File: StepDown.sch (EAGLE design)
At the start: 18 parts, among them IC1 TL494CN, T1 TIP32A

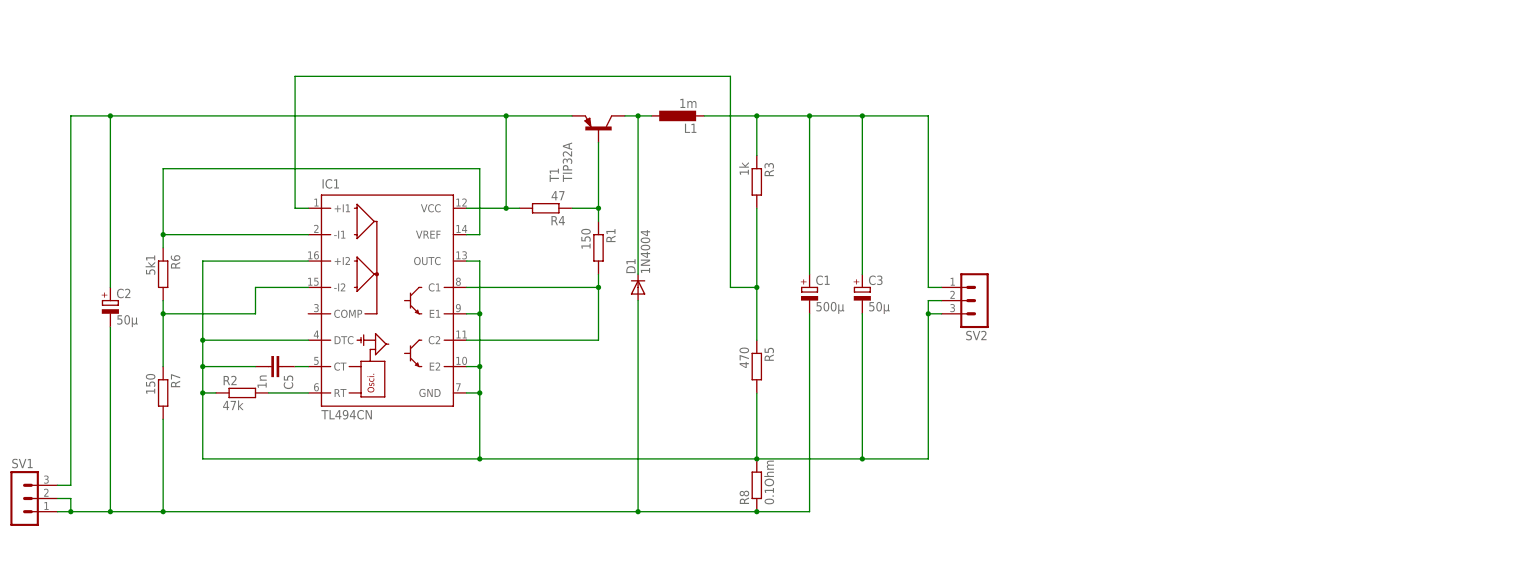
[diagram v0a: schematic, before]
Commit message: Add current sense (not tested)
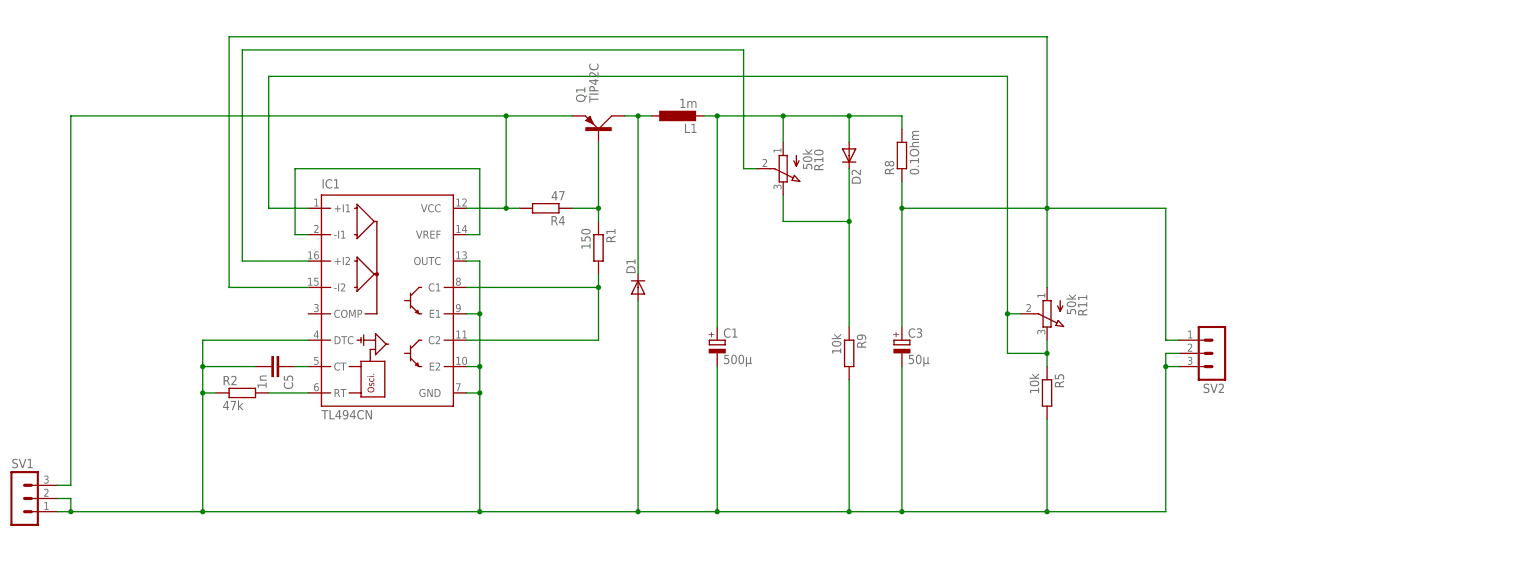
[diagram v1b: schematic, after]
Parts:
- removed C2: 50µ, rcl:CPOL-EUE5-8.5
- removed R3: 1k, rcl:R-EU_0204/2V
- removed R6: 5k1, rcl:R-EU_0204/2V
- removed R7: 150, rcl:R-EU_0204/2V
- removed T1: TIP32A, transistor:TIP32A
- added D2: (no value), diode:DIODE-D-2.5
- added Q1: TIP42C, transistor-power:TIP42C
- added R10, R11: 50k, pot:EVUE2A
- added R9: 10k, rcl:R-EU_0204/2V
- C3: device rcl:CPOL-EUE5-8.5 -> rcl:CPOL-EUE2.5-7
- D1: value 1N4004 -> (none); device diode:1N4004 -> diode:DIODE-D-2.5
- R5: value 470 -> 10k
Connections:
- removed net N$14: C3.-, C5.2, IC1.+I2, IC1.DTC, IC1.E1, IC1.E2, IC1.GND, IC1.OUTC, R2.1, R5.2, R8.2, SV2.2, SV2.3
- new net N$12: C1.-, C3.-, C5.2, D1.A, IC1.DTC, IC1.E1, IC1.E2, IC1.GND, IC1.OUTC, R2.1, R5.2, R9.2, SV1.1, SV1.2, SV2.2, SV2.3
- new net N$4: C1.+, D2.A, L1.2, R10.A, R8.2
- net N$1: now also Q1.E; no longer C2.+, T1.E
- net N$10: now also IC1.-I2, R11.A, R8.1; no longer C1.+, L1.2, R3.1
- net N$11: now also R11.E, R11.S; no longer R3.2
- net N$13: now also D2.C, R10.E, R9.1; no longer IC1.-I2, R6.2, R7.1
- net N$3: no longer R6.1
- net N$5: now also IC1.+I2, R10.S; no longer C1.-, C2.-, D1.A, R7.2, R8.1, SV1.1, SV1.2
- net N$7: now also Q1.B; no longer T1.B
- net N$9: now also Q1.C; no longer T1.C
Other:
- moved on the sheet: C1, C3, R5, R8, SV2

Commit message: Use MOSFET for more than 25A (tested and working)
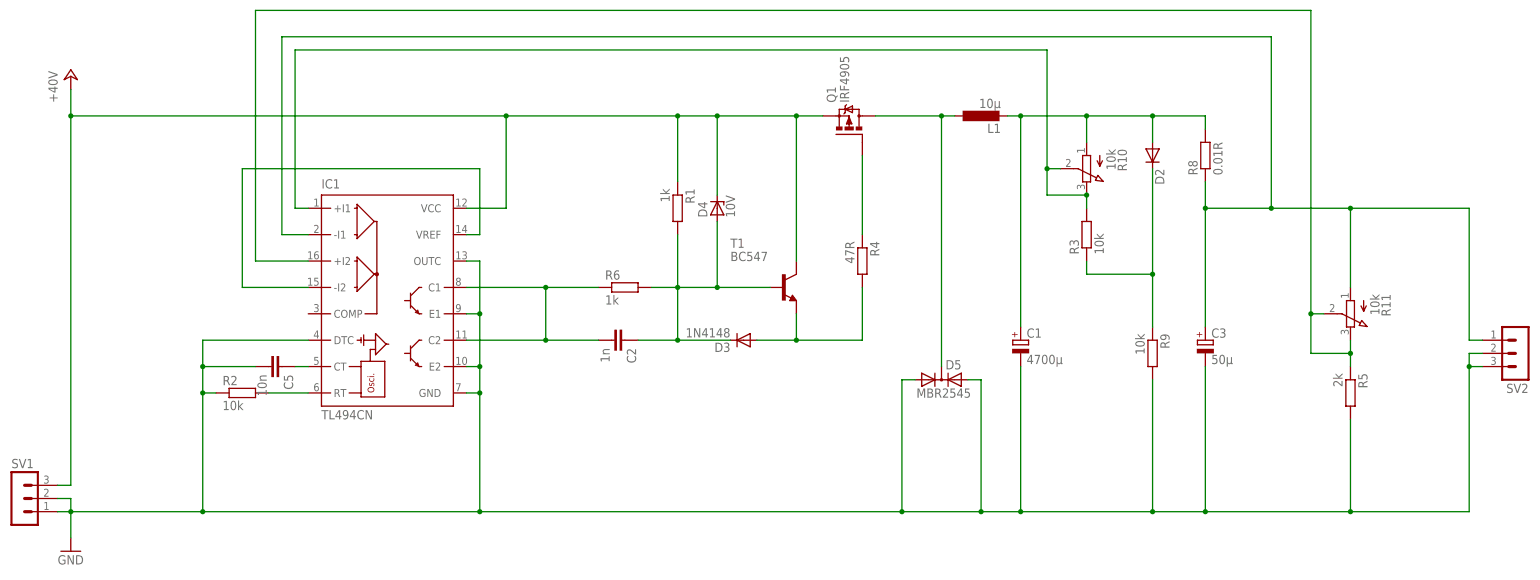
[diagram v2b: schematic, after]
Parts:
- removed D1: (no value), diode:DIODE-D-2.5
- added C2: 1n, rcl:C-EU025-040X050
- added D3: 1N4148, diode:DIODE-D-2.5
- added D4: 10V, diode:ZENER-DIODEZD-2.5
- added D5: MBR2545, diode:DIODE-2AC|CATO3P
- added R3: 10k, rcl:R-EU_0204/2V
- added R6: 1k, rcl:R-EU_0204/2V
- added T1: BC547, transistor:BC547-NPN-TO92-CBE
- C1: value 500µ -> 4700µ; device rcl:CPOL-EUE5-8.5 -> rcl:CPOL-EUE10-20
- C5: value 1n -> 10n; device rcl:C-EU025-040X050 -> rcl:C-EU075-032X103
- D2: device diode:DIODE-D-2.5 -> diode:DIODE-D-10
- L1: value 1m -> 10µ; device rcl:L-EU6000-XXX-RC -> rcl:L-EUTFI0307
- Q1: value TIP42C -> IRF4905; device transistor-power:TIP42C -> transistor-power:IRF4905
- R1: value 150 -> 1k
- R10, R11: value 50k -> 10k
- R2: value 47k -> 10k
- R4: value 47 -> 47R
- R5: value 10k -> 2k; device rcl:R-EU_0204/2V -> rcl:R-EU_0207/12
- R8: value 0.1Ohm -> 0.01R; device rcl:R-EU_0309/10 -> rcl:R-EU_0617/5V
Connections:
- removed net N$12: C1.-, C3.-, C5.2, D1.A, IC1.DTC, IC1.E1, IC1.E2, IC1.GND, IC1.OUTC, R2.1, R5.2, R9.2, SV1.1, SV1.2, SV2.2, SV2.3
- new net +24V: D4.C, IC1.VCC, Q1.S, R1.1, SV1.3, T1.C
- new net GND: C1.-, C3.-, C5.2, D5.A1, D5.A2, IC1.DTC, IC1.E1, IC1.E2, IC1.GND, IC1.OUTC, R2.1, R5.2, R9.2, SV1.1, SV1.2, SV2.2, SV2.3
- new net N$14: Q1.G, R4.1
- net N$1: now also C2.2, IC1.C1, IC1.C2, R6.1; no longer IC1.VCC, Q1.E, R4.2, SV1.3
- net N$10: now also IC1.-I1; no longer IC1.-I2
- net N$11: now also IC1.+I2; no longer IC1.+I1
- net N$13: now also R3.1; no longer R10.E
- net N$3: now also IC1.-I2; no longer IC1.-I1
- net N$5: now also IC1.+I1, R10.E, R3.2; no longer IC1.+I2
- net N$7: now also D3.A, R4.2, T1.E; no longer Q1.B, R1.1, R4.1
- net N$8: now also C2.1, D3.C, D4.A, R6.2, T1.B; no longer IC1.C1, IC1.C2
- net N$9: now also D5.C, Q1.D; no longer D1.C, Q1.C
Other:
- moved on the sheet: C1, C3, D2, L1, R1, R10, R11, R4, R5, R8, R9, SV2
